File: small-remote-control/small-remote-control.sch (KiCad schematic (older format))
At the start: 11 parts

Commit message: Started PCB
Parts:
- removed R?: 0Ω, symbol Device:R_Small_US
- J1, J2: renamed from J?; footprint (none) -> SW-Tensility:54-00174; Description (none) -> CONN JACK 4COND 3.5MM R/A; MPN (none) -> 54-00174; Manufacturer (none) -> Tensility International Corp; Source (none) -> Digikey
- MK1: renamed from MK?; footprint (none) -> SW-CUI-INC:CMC-4015-40P; Characteristics (none) -> (-40dB ±3dB @ 94dB SPL); Description (none) -> 100Hz ~ 20kHz Analog Microphone Electret Condenser 2V ~ 10V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; MPN EM-4015PR-38 -> CMC-4015-40P; Manufacturer Soberton Inc -> CUI Devices
- R1: renamed from R?; value R_Small_US -> 267Ω ±0.1%; footprint (none) -> Resistor_SMD:R_0402_1005Metric; Characteristics (none) -> 0.1% 1/10W; Description (none) -> RES 267 OHM 0.1% 1/10W 0402; MPN (none) -> RP73PF1E267RBTD; Manufacturer (none) -> TE Connectivity; Package ID (none) -> 0402/1005M; Source (none) -> Digikey
- R2: renamed from R?; value R_Small_US -> 604Ω ±0.1%; footprint (none) -> Resistor_SMD:R_0402_1005Metric; Characteristics (none) -> 0.1% 1/10W; Description (none) -> RES 604 OHM 0.1% 1/10W 0402; MPN (none) -> RP73PF1E604RBTD; Manufacturer (none) -> TE Connectivity; Package ID (none) -> 0402/1005M; Source (none) -> Digikey
- R3: renamed from R?; value R_Small_US -> 143Ω ±0.1%; footprint (none) -> Resistor_SMD:R_0402_1005Metric; Characteristics (none) -> 0.1% 1/10W; Description (none) -> RES 143 OHM 0.1% 1/10W 0402; MPN (none) -> RP73PF1E143RBTD; Manufacturer (none) -> TE Connectivity; Package ID (none) -> 0402/1005M; Source (none) -> Digikey
- SW1: renamed from SW?; value SW_Push -> A; footprint (none) -> SW-Omron:B3W-6x6mm-NG; Description (none) -> SWITCH TACTILE SPST-NO 0.05A 24V; MPN (none) -> B3W-1002; Manufacturer (none) -> Omron Electronics Inc-EMC Div; Source (none) -> Digikey
- SW2: renamed from SW?; value SW_Push -> B; footprint (none) -> SW-Omron:B3W-6x6mm-NG; Description (none) -> SWITCH TACTILE SPST-NO 0.05A 24V; MPN (none) -> B3W-1002; Manufacturer (none) -> Omron Electronics Inc-EMC Div; Source (none) -> Digikey
- SW3: renamed from SW?; value SW_Push -> C; footprint (none) -> SW-Omron:B3W-6x6mm-NG; Description (none) -> SWITCH TACTILE SPST-NO 0.05A 24V; MPN (none) -> B3W-1002; Manufacturer (none) -> Omron Electronics Inc-EMC Div; Source (none) -> Digikey
- SW4: renamed from SW?; value SW_Push -> D; footprint (none) -> SW-Omron:B3W-6x6mm-NG; Description (none) -> SWITCH TACTILE SPST-NO 0.05A 24V; MPN (none) -> B3W-1002; Manufacturer (none) -> Omron Electronics Inc-EMC Div; Source (none) -> Digikey
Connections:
- net MIC: now also SW1.1
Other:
- note added: "Req=(Rmic *R)/(Rmic+R)\n\nIdeal values\nReqA = 0Ω\nReqB = 240Ω\nReqC = 470Ω\nReqD = 135Ω\nRmic = 2k2Ω\n\nRange\n\nReqA < 70Ω\n210Ω < ReqB < 290Ω\n360Ω < ReqC < 680Ω\n110Ω < ReqD < 180Ω\n\nCalculated with Rmic = 2k2Ω\nRA=0Ω\nRB = ~~269.39Ω\nRC = ~~597.69Ω\nRD = ~~143.83Ω\n\nClosest E96 and actual Req\n\nRA = 0Ω / ReqA = 0Ω\nRB = 267Ω / ReqB = 238.1Ω\nRC = 604Ω / ReqC = 473.9Ω\nRD = 143Ω / ReqD = 1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"
- note removed: "Req=(Rmic *R)/(Rmic+R)\nReqA = 0Ω\nReqB = 240Ω\nReqC = 470Ω\nReqD = 135Ω\nRmic = 2k2Ω\n\nRA=0\nRB = ~~269.39\nRC = ~~597.69\nRD = ~~143.83"
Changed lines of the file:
@@
 EESchema Schematic File Version 4
+LIBS:small-remote-control-cache
 EELAYER 30 0
 EELAYER END
@@
 $EndDescr
 $Comp
-L Switch:SW_Push SW?
+L Switch:SW_Push SW1
 U 1 1 5F24E03E
 P 2950 3350
-F 0 "SW?" H 3000 3450 50  0000 L CNN
-F 1 "SW_Push" H 2950 3290 50  0000 C CNN
-F 2 "" H 2950 3550 50  0001 C CNN
-F 3 "~" H 2950 3550 50  0001 C CNN
+F 0 "SW1" H 3000 3450 50  0000 L CNN
+F 1 "A" H 2950 3290 50  0000 C CNN
+F 2 "SW-Omron:B3W-6x6mm-NG" H 2950 3550 50  0001 C CNN
+F 3 "https://omronfs.omron.com/en_US/ecb/products/pdf/en-b3w.pdf" H 2950 3550 50  0001 C CNN
+F 4 "B3W-1002" H 2950 3350 50  0001 C CNN "MPN"
+F 5 "SWITCH TACTILE SPST-NO 0.05A 24V" H 2950 3350 50  0001 C CNN "Description"
+F 6 "Omron Electronics Inc-EMC Div" H 2950 3350 50  0001 C CNN "Manufacturer"
+F 7 "Digikey" H 2950 3350 50  0001 C CNN "Source"
 	1    2950 3350
 	0    -1   1    0
 $EndComp
 $Comp
-L Switch:SW_Push SW?
+L Switch:SW_Push SW2
 U 1 1 5F24EBE2
 P 3500 3350
-F 0 "SW?" H 3550 3450 50  0000 L CNN
-F 1 "SW_Push" H 3500 3290 50  0000 C CNN
-F 2 "" H 3500 3550 50  0001 C CNN
-F 3 "~" H 3500 3550 50  0001 C CNN
+F 0 "SW2" H 3550 3450 50  0000 L CNN
+F 1 "B" H 3500 3290 50  0000 C CNN
+F 2 "SW-Omron:B3W-6x6mm-NG" H 3500 3550 50  0001 C CNN
+F 3 "https://omronfs.omron.com/en_US/ecb/products/pdf/en-b3w.pdf" H 3500 3550 50  0001 C CNN
+F 4 "B3W-1002" H 3500 3350 50  0001 C CNN "MPN"
+F 5 "SWITCH TACTILE SPST-NO 0.05A 24V" H 3500 3350 50  0001 C CNN "Description"
+F 6 "Omron Electronics Inc-EMC Div" H 3500 3350 50  0001 C CNN "Manufacturer"
+F 7 "Digikey" H 3500 3350 50  0001 C CNN "Source"
 	1    3500 3350
 	0    -1   1    0
 $EndComp
 $Comp
-L Switch:SW_Push SW?
+L Switch:SW_Push SW3
 U 1 1 5F24F6DC
 P 4050 3350
-F 0 "SW?" H 4100 3450 50  0000 L CNN
-F 1 "SW_Push" H 4050 3290 50  0000 C CNN
-F 2 "" H 4050 3550 50  0001 C CNN
-F 3 "~" H 4050 3550 50  0001 C CNN
+F 0 "SW3" H 4100 3450 50  0000 L CNN
+F 1 "C" H 4050 3290 50  0000 C CNN
+F 2 "SW-Omron:B3W-6x6mm-NG" H 4050 3550 50  0001 C CNN
+F 3 "https://omronfs.omron.com/en_US/ecb/products/pdf/en-b3w.pdf" H 4050 3550 50  0001 C CNN
+F 4 "B3W-1002" H 4050 3350 50  0001 C CNN "MPN"
+F 5 "SWITCH TACTILE SPST-NO 0.05A 24V" H 4050 3350 50  0001 C CNN "Description"
+F 6 "Omron Electronics Inc-EMC Div" H 4050 3350 50  0001 C CNN "Manufacturer"
+F 7 "Digikey" H 4050 3350 50  0001 C CNN "Source"
 	1    4050 3350
 	0    -1   1    0
 $EndComp
 $Comp
-L Switch:SW_Push SW?
+L Switch:SW_Push SW4
 U 1 1 5F24FFE6
 P 4600 3350
-F 0 "SW?" H 4650 3450 50  0000 L CNN
-F 1 "SW_Push" H 4600 3290 50  0000 C CNN
-F 2 "" H 4600 3550 50  0001 C CNN
-F 3 "~" H 4600 3550 50  0001 C CNN
+F 0 "SW4" H 4650 3450 50  0000 L CNN
+F 1 "D" H 4600 3290 50  0000 C CNN
+F 2 "SW-Omron:B3W-6x6mm-NG" H 4600 3550 50  0001 C CNN
+F 3 "https://omronfs.omron.com/en_US/ecb/products/pdf/en-b3w.pdf" H 4600 3550 50  0001 C CNN
+F 4 "B3W-1002" H 4600 3350 50  0001 C CNN "MPN"
+F 5 "SWITCH TACTILE SPST-NO 0.05A 24V" H 4600 3350 50  0001 C CNN "Description"
+F 6 "Omron Electronics Inc-EMC Div" H 4600 3350 50  0001 C CNN "Manufacturer"
+F 7 "Digikey" H 4600 3350 50  0001 C CNN "Source"
 	1    4600 3350
 	0    -1   1    0
 $EndComp
 $Comp
-L Device:Microphone MK?
+L Device:Microphone MK1
 U 1 1 5F25357C
 P 5300 3150
-F 0 "MK?" H 5150 3200 50  0000 R CNN
+F 0 "MK1" H 5150 3200 50  0000 R CNN
 F 1 "Microphone" H 5150 3125 50  0000 R CNN
-F 2 "" V 5300 3250 50  0001 C CNN
-F 3 "~" V 5300 3250 50  0001 C CNN
-F 4 "Soberton Inc" H 5300 3150 50  0001 C CNN "Manufacturer"
+F 2 "SW-CUI-INC:CMC-4015-40P" V 5300 3250 50  0001 C CNN
+F 3 "https://www.cuidevices.com/product/resource/cmc-4015-40p.pdf" V 5300 3250 50  0001 C CNN
+F 4 "CUI Devices" H 5300 3150 50  0001 C CNN "Manufacturer"
 F 5 "Digikey" H 5300 3150 50  0001 C CNN "Source"
-F 6 "EM-4015PR-38" H 5300 3150 50  0001 C CNN "MPN"
+F 6 "CMC-4015-40P" H 5300 3150 50  0001 C CNN "MPN"
+F 7 "(-40dB ±3dB @ 94dB SPL)" H 5300 3150 50  0001 C CNN "Characteristics"
+F 8 "100Hz ~ 20kHz Analog Microphone Electret Condenser 2V ~ 10V Omnidirectional (-40dB ±3dB @ 94dB SPL) PC Pins" H 5300 3150 50  0001 C CNN "Description"
 	1    5300 3150
 	-1   0    0    1
 $EndComp
 $Comp
-L Device:R_Small_US R?
-U 1 1 5F2540F0
-P 2950 2900
-F 0 "R?" H 2980 2920 50  0000 L CNN
-F 1 "0Ω" H 2980 2860 50  0000 L CNN
-F 2 "" H 2950 2900 50  0001 C CNN
-F 3 "~" H 2950 2900 50  0001 C CNN
-	1    2950 2900
-	1    0    0    1
-$EndComp
-$Comp
-L Device:R_Small_US R?
+L Device:R_Small_US R1
 U 1 1 5F254652
 P 3500 2900
-F 0 "R?" H 3530 2920 50  0000 L CNN
-F 1 "R_Small_US" H 3530 2860 50  0000 L CNN
-F 2 "" H 3500 2900 50  0001 C CNN
+F 0 "R1" H 3530 2920 50  0000 L CNN
+F 1 "267Ω ±0.1%" H 3530 2860 50  0000 L CNN
+F 2 "Resistor_SMD:R_0402_1005Metric" H 3500 2900 50  0001 C CNN
 F 3 "~" H 3500 2900 50  0001 C CNN
+F 4 "RES 267 OHM 0.1% 1/10W 0402" H 3500 2900 50  0001 C CNN "Description"
+F 5 "RP73PF1E267RBTD" H 3500 2900 50  0001 C CNN "MPN"
+F 6 "TE Connectivity" H 3500 2900 50  0001 C CNN "Manufacturer"
+F 7 "0402/1005M" H 3500 2900 50  0001 C CNN "Package ID"
+F 8 "Digikey" H 3500 2900 50  0001 C CNN "Source"
+F 9 "0.1% 1/10W" H 3500 2900 50  0001 C CNN "Characteristics"
 	1    3500 2900
 	1    0    0    1
 $EndComp
 $Comp
-L Device:R_Small_US R?
+L Device:R_Small_US R2
 U 1 1 5F2548F5
 P 4050 2900
-F 0 "R?" H 4080 2920 50  0000 L CNN
-F 1 "R_Small_US" H 4080 2860 50  0000 L CNN
-F 2 "" H 4050 2900 50  0001 C CNN
+F 0 "R2" H 4080 2920 50  0000 L CNN
+F 1 "604Ω ±0.1%" H 4080 2860 50  0000 L CNN
+F 2 "Resistor_SMD:R_0402_1005Metric" H 4050 2900 50  0001 C CNN
 F 3 "~" H 4050 2900 50  0001 C CNN
+F 4 "RES 604 OHM 0.1% 1/10W 0402" H 4050 2900 50  0001 C CNN "Description"
+F 5 "RP73PF1E604RBTD" H 4050 2900 50  0001 C CNN "MPN"
+F 6 "TE Connectivity" H 4050 2900 50  0001 C CNN "Manufacturer"
+F 7 "0402/1005M" H 4050 2900 50  0001 C CNN "Package ID"
+F 8 "Digikey" H 4050 2900 50  0001 C CNN "Source"
+F 9 "0.1% 1/10W" H 4050 2900 50  0001 C CNN "Characteristics"
 	1    4050 2900
 	1    0    0    1
 $EndComp
 $Comp
-L Device:R_Small_US R?
+L Device:R_Small_US R3
 U 1 1 5F254B04
 P 4600 2900
-F 0 "R?" H 4630 2920 50  0000 L CNN
-F 1 "R_Small_US" H 4630 2860 50  0000 L CNN
-F 2 "" H 4600 2900 50  0001 C CNN
+F 0 "R3" H 4630 2920 50  0000 L CNN
+F 1 "143Ω ±0.1%" H 4630 2860 50  0000 L CNN
+F 2 "Resistor_SMD:R_0402_1005Metric" H 4600 2900 50  0001 C CNN
 F 3 "~" H 4600 2900 50  0001 C CNN
+F 4 "TE Connectivity" H 4600 2900 50  0001 C CNN "Manufacturer"
+F 5 "0402/1005M" H 4600 2900 50  0001 C CNN "Package ID"
+F 6 "Digikey" H 4600 2900 50  0001 C CNN "Source"
+F 7 "RP73PF1E143RBTD" H 4600 2900 50  0001 C CNN "MPN"
+F 8 "RES 143 OHM 0.1% 1/10W 0402" H 4600 2900 50  0001 C CNN "Description"
+F 9 "0.1% 1/10W" H 4600 2900 50  0001 C CNN "Characteristics"
 	1    4600 2900
 	1    0    0    1
@@
 Text Notes 900  3350 0    50   ~ 0
 CTIA pinout
-Text Notes 3500 4750 0    50   ~ 0
-Req=(Rmic *R)/(Rmic+R)\nReqA = 0Ω\nReqB = 240Ω\nReqC = 470Ω\nReqD = 135Ω\nRmic = 2k2Ω\n\nRA=0\nRB = ~~269.39\nRC = ~~597.69\nRD = ~~143.83
+Text Notes 8000 4400 0    50   ~ 0
+Req=(Rmic *R)/(Rmic+R)\n\nIdeal values\nReqA = 0Ω\nReqB = 240Ω\nReqC = 470Ω\nReqD = 135Ω\nRmic = 2k2Ω\n\nRange\n\nReqA < 70Ω\n210Ω < ReqB < 290Ω\n360Ω < ReqC < 680Ω\n110Ω < ReqD < 180Ω\n\nCalculated with Rmic = 2k2Ω\nRA=0Ω\nRB = ~~269.39Ω\nRC = ~~597.69Ω\nRD = ~~143.83Ω\n\nClosest E96 and actual Req\n\nRA = 0Ω / ReqA = 0Ω\nRB = 267Ω / ReqB = 238.1Ω\nRC = 604Ω / ReqC = 473.9Ω\nRD = 143Ω / ReqD = 134.3Ω
 Wire Wire Line
 	4600 2750 4600 2800
@@
 Wire Wire Line
 	3500 2750 4050 2750
-Wire Wire Line
-	2950 2800 2950 2750
 Connection ~ 2950 2750
 Wire Wire Line
@@
 Wire Wire Line
 	3500 3150 3500 3000
-Wire Wire Line
-	2950 3150 2950 3000
-$Comp
-L Connector:AudioJack4 J?
+$Comp
+L Connector:AudioJack4 J1
 U 1 1 5F25DFB2
 P 1200 2850
-F 0 "J?" H 1200 3200 50  0000 C CNN
+F 0 "J1" H 1200 3200 50  0000 C CNN
 F 1 "AudioJack4" H 1200 3100 50  0000 C CNN
-F 2 "" H 1200 2850 50  0001 C CNN
-F 3 "~" H 1200 2850 50  0001 C CNN
+F 2 "SW-Tensility:54-00174" H 1200 2850 50  0001 C CNN
+F 3 "https://tensility.s3-us-west-2.amazonaws.com/uploads/product_doc/document/4372/54-00174.pdf" H 1200 2850 50  0001 C CNN
+F 4 "CONN JACK 4COND 3.5MM R/A" H 1200 2850 50  0001 C CNN "Description"
+F 5 "54-00174" H 1200 2850 50  0001 C CNN "MPN"
+F 6 "Tensility International Corp" H 1200 2850 50  0001 C CNN "Manufacturer"
+F 7 "Digikey" H 1200 2850 50  0001 C CNN "Source"
 	1    1200 2850
 	1    0    0    -1
 $EndComp
 $Comp
-L Connector:AudioJack4 J?
+L Connector:AudioJack4 J2
 U 1 1 5F25F27A
 P 6500 2850
-F 0 "J?" H 6500 3200 50  0000 C CNN
+F 0 "J2" H 6500 3200 50  0000 C CNN
 F 1 "AudioJack4" H 6500 3100 50  0000 C CNN
-F 2 "" H 6500 2850 50  0001 C CNN
-F 3 "~" H 6500 2850 50  0001 C CNN
+F 2 "SW-Tensility:54-00174" H 6500 2850 50  0001 C CNN
+F 3 "https://tensility.s3-us-west-2.amazonaws.com/uploads/product_doc/document/4372/54-00174.pdf" H 6500 2850 50  0001 C CNN
+F 4 "CONN JACK 4COND 3.5MM R/A" H 6500 2850 50  0001 C CNN "Description"
+F 5 "54-00174" H 6500 2850 50  0001 C CNN "MPN"
+F 6 "Tensility International Corp" H 6500 2850 50  0001 C CNN "Manufacturer"
+F 7 "Digikey" H 6500 2850 50  0001 C CNN "Source"
 	1    6500 2850
 	-1   0    0    -1
@@
 	5700 2850 6300 2850
 Connection ~ 5300 3650
+Wire Wire Line
+	2950 2750 2950 3150
 $EndSCHEMATC

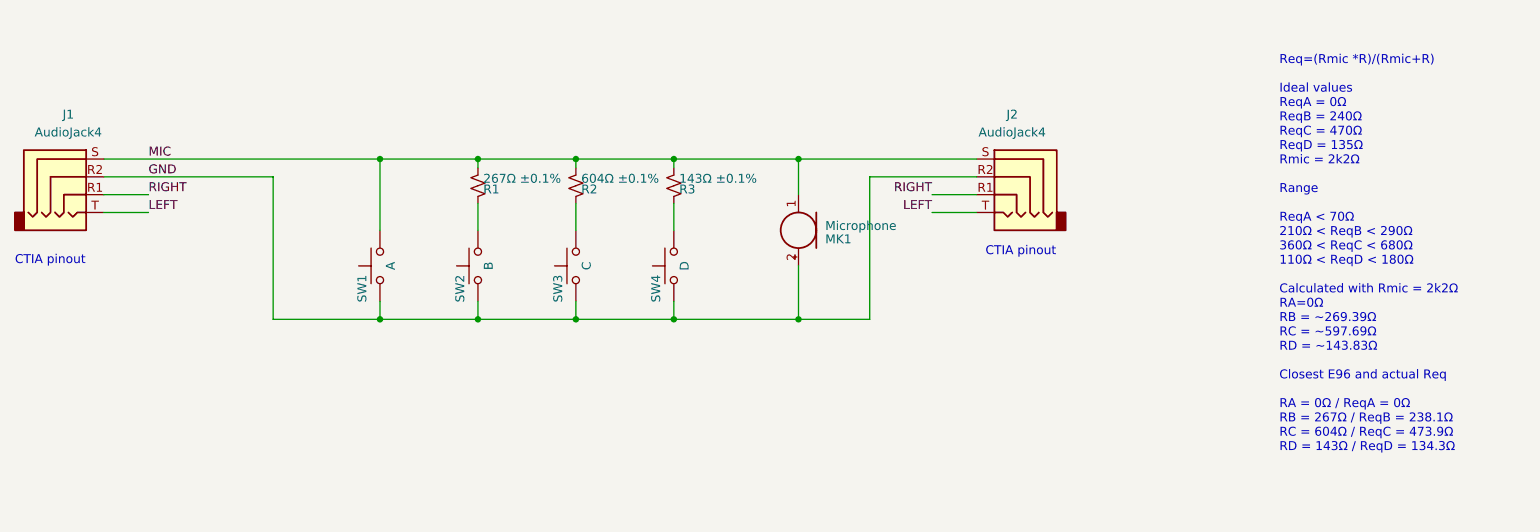
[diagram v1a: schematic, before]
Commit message: removed feedthrough jack and moved switches closer
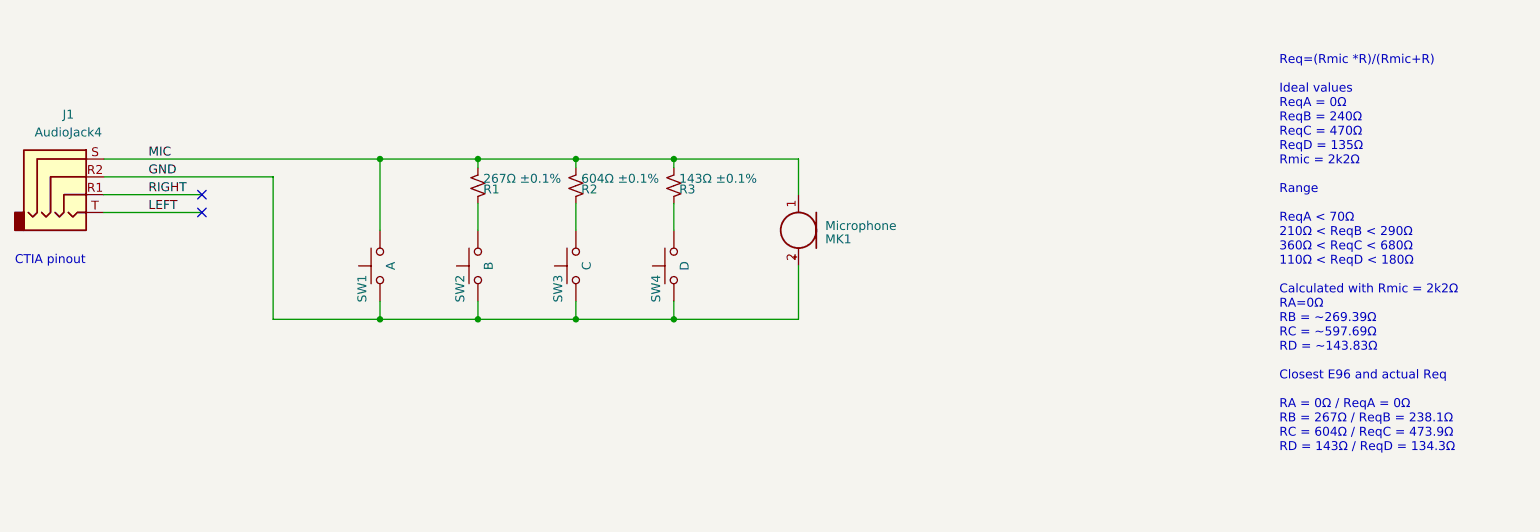
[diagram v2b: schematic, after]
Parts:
- removed J2: AudioJack4, SW-Tensility:54-00174, symbol Connector:AudioJack4
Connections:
- no-connect marks 0 -> 2
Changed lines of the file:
@@
 Text Label 1650 2750 0    50   ~ 0
 MIC
-Wire Wire Line
-	1400 3050 1650 3050
-Wire Wire Line
-	1400 2950 1650 2950
 Text Notes 900  3350 0    50   ~ 0
 CTIA pinout
@@
 	1    0    0    -1
 $EndComp
-$Comp
-L Connector:AudioJack4 J2
-U 1 1 5F25F27A
-P 6500 2850
-F 0 "J2" H 6500 3200 50  0000 C CNN
-F 1 "AudioJack4" H 6500 3100 50  0000 C CNN
-F 2 "SW-Tensility:54-00174" H 6500 2850 50  0001 C CNN
-F 3 "https://tensility.s3-us-west-2.amazonaws.com/uploads/product_doc/document/4372/54-00174.pdf" H 6500 2850 50  0001 C CNN
-F 4 "CONN JACK 4COND 3.5MM R/A" H 6500 2850 50  0001 C CNN "Description"
-F 5 "54-00174" H 6500 2850 50  0001 C CNN "MPN"
-F 6 "Tensility International Corp" H 6500 2850 50  0001 C CNN "Manufacturer"
-F 7 "Digikey" H 6500 2850 50  0001 C CNN "Source"
-	1    6500 2850
-	-1   0    0    -1
-$EndComp
-Text Notes 6350 3300 0    50   ~ 0
-CTIA pinout
-Text Label 6050 3050 2    50   ~ 0
-LEFT
-Text Label 6050 2950 2    50   ~ 0
-RIGHT
-Wire Wire Line
-	6300 3050 6050 3050
-Wire Wire Line
-	6300 2950 6050 2950
-Wire Wire Line
-	5300 2750 6300 2750
-Connection ~ 5300 2750
-Wire Wire Line
-	5300 3650 5700 3650
-Wire Wire Line
-	5700 3650 5700 2850
-Wire Wire Line
-	5700 2850 6300 2850
-Connection ~ 5300 3650
 Wire Wire Line
 	2950 2750 2950 3150
+NoConn ~ 1950 2950
+NoConn ~ 1950 3050
+Wire Wire Line
+	1400 3050 1950 3050
+Wire Wire Line
+	1400 2950 1950 2950
 $EndSCHEMATC
